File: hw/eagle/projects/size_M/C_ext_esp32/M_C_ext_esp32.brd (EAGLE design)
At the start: 19 parts, among them IC1 CP2102

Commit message: pcb M.1 -not finished
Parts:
- removed C1, C2, C4: 100n, rcl:C0603
- removed C3: 0.1F, rcl:C0603
- removed C5: 10u, rcl:C0603
- removed C6: 2u2, rcl:C0603
- removed IC1: CP2102, silabs:MLP28
- removed R1, R2: 2k2, rcl:R0603
- removed R3, R4, R5, R6: 12k, rcl:R0603
- removed T1, T2: (no value), transistor:SOT23-BEC
- removed USB: MICRO-USB, hugo:MICRO-USB
- added C.C1, C.C2, C.C4: 100n, rcl:C0603
- added C.C3: 22u, rcl:C0805
- added C.C5: 10u, rcl:C0603
- added C.C6: 2u2, rcl:C0603
- added C.R1, C.R2: 2k2, rcl:R0603
- added C.R3, C.R4, C.R5, C.R6: 12k, rcl:R0603
- added C.U1: TTGO-MICRO-32, hugo:TTGO-MICRO-32
- added C.U3: BC817DS,115, SamacSys_Parts:SOT95P275X110-6N
- added U1: CP2104-F03-GM, CP2104:QFN50P400X400X80-25N
- JP1: device pinhead2:1X02 -> pinhead2:1X04
- U$1: value TTGO-MICRO-32 -> USB-C; device hugo:TTGO-MICRO-32 -> hugo:USB-C
- moved U$1 8.85 mm to (10.5, 18.4), flipped to the bottom
- moved JP1 2.53 mm to (19.6, 10.5)
- renumbered JP2 to C.J2
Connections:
- removed net VDD: C1.1, C2.1, C3.1, IC1.6, R1.2, R2.2, R5.2, R6.1, U$1.3V3
- new net VCC: C.C1.1, C.C2.1, C.C3.1, C.R1.2, C.R2.2, C.R5.2, C.R6.1, C.U1.3V3, JP1.3, U1.6
- new net VIO: U1.5
- net GND: now also C.C1.2, C.C2.2, C.C3.2, C.C4.1, C.C5.1, C.C6.2, C.U1.GND1, C.U1.GND10, C.U1.GND11, C.U1.GND2, C.U1.GND3, C.U1.GND4, C.U1.GND5, C.U1.GND6, C.U1.GND7, C.U1.GND8, C.U1.GND9, JP1.4, U$1.A1B12, U$1.B1A12, U$1.SH1, U$1.SH2, U$1.SH3, U$1.SH4, U1.2, U1.25; no longer C1.2, C2.2, C3.2, C4.1, C5.1, C6.2, IC1.3, IC1.EXP, IC1.M, U$1.GND1, U$1.GND2, U$1.GND3, U$1.GND4, USB.GND, USB.GND1, USB.GND2, USB.GND3, USB.GND4, USB.P$1, USB.P$2
- net N$1: now also U$1.A7, U1.4; no longer IC1.5, USB.D-
- net N$10: now also C.R5.1, C.U1.IO0, C.U3.3; no longer R5.1, T2.C, U$1.IO0
- net N$11: now also C.C6.1, C.R6.2, C.U1.EN, C.U3.6; no longer C6.1, R6.2, T1.C, U$1.EN
- net N$13: now also C.U1.IO2; no longer U$1.IO2
- net N$2: now also U$1.A6, U1.3; no longer IC1.4, USB.D+
- net N$5: now also C.R4.2, C.U3.5; no longer R4.2, T1.B
- net N$7: now also C.R3.2, C.U3.2; no longer R3.2, T2.B
- net N$8: now also C.R3.1, C.U3.4, U1.19; no longer IC1.9, R3.1, T1.E
- net N$9: now also C.R4.1, C.U3.1, U1.23; no longer IC1.28, R4.1, T2.E
- net RX: now also C.U1.RXD0, U1.20; no longer IC1.25, U$1.RXD0
- net SCL: now also C.R1.1, C.U1.IO22; no longer R1.1, U$1.IO22
- net SDA: now also C.R2.1, C.U1.IO21; no longer R2.1, U$1.IO21
- net TX: now also C.U1.TXD0, U1.21; no longer IC1.26, U$1.TXD0
- net VUSB: now also C.C4.2, C.C5.2, U$1.A4B9, U$1.B4A9, U1.7, U1.8; no longer C4.2, C5.2, IC1.7, IC1.8, USB.VUSB
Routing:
- net VCC: track 0.00 -> 56.4 mm
- net VDD: track 54.9 -> 0.00 mm, vias 5 -> 0
- net N$11: track 23.4 -> 12.9 mm, vias 1 -> 2
- net N$10: track 9.96 -> 19.7 mm, vias 1 -> 2
- net GND: track 111.2 -> 119.3 mm, vias 4 -> 6
- net RX: track 13.1 -> 5.41 mm
- net N$1: track 9.82 -> 2.26 mm, vias 2 -> 0
- net VUSB: track 22.7 -> 29.8 mm, vias 2 -> 3
- net N$2: track 9.08 -> 2.25 mm
- net TX: track 12.0 -> 7.57 mm
- net N$7: track 4.91 -> 2.24 mm
- net N$9: track 13.5 -> 14.6 mm
- net N$8: track 11.2 -> 12.3 mm, vias 0 -> 2
- net N$5: track 2.51 -> 3.22 mm
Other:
- board text added: "ESP M.1"
- board text removed: "esp M.0"

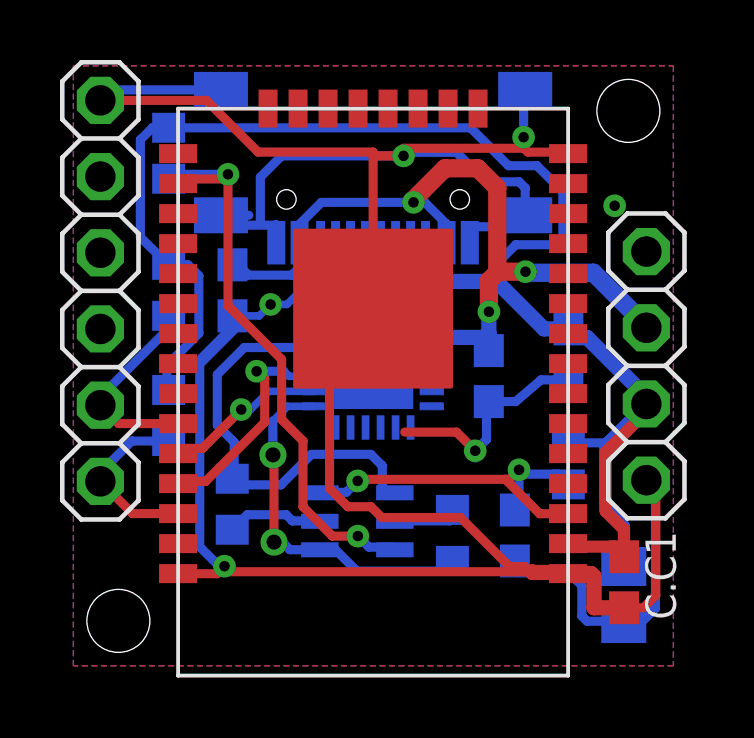
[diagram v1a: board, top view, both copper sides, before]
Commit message: updateed PCBs - adjustments based on usage of version 1
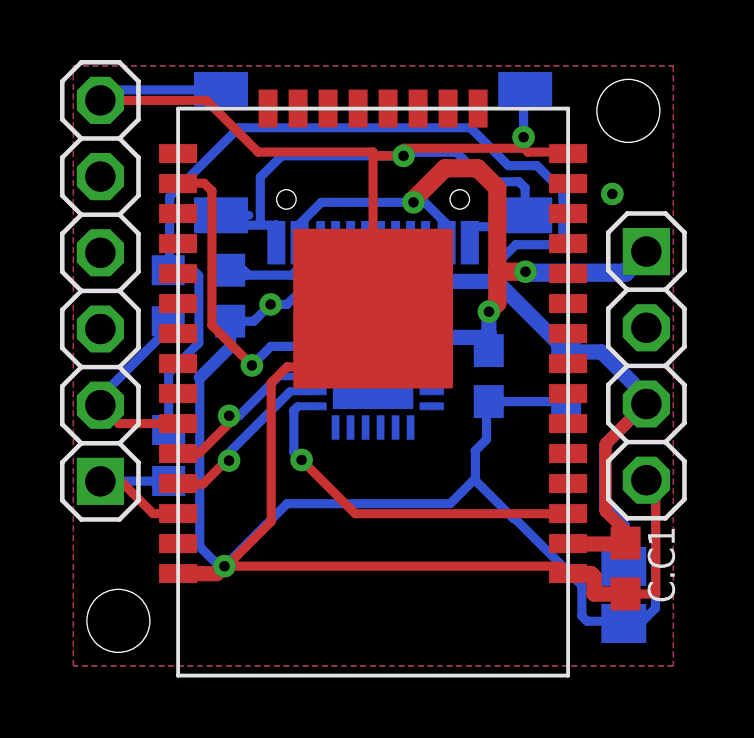
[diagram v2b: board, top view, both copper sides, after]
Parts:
- removed C.C6: 2u2, rcl:C0603
- removed C.R3, C.R4, C.R5, C.R6: 12k, rcl:R0603
- removed C.U3: BC817DS,115, SamacSys_Parts:SOT95P275X110-6N
- moved C.R1 1.33 mm to (3.68, 7.51)
- moved C.C2 0.74 mm to (16.9, 10.1)
- moved C.C1 0.46 mm to (18.9, 3.74)
- moved C.C5 0.19 mm to (5.73, 12.8)
- moved C.R2 0.18 mm to (3.66, 12.8)
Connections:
- removed net N$10: C.R5.1, C.U1.IO0, C.U3.3
- removed net N$11: C.C6.1, C.R6.2, C.U1.EN, C.U3.6
- removed net N$13: C.U1.IO2
- removed net N$5: C.R4.2, C.U3.5
- removed net N$7: C.R3.2, C.U3.2
- removed net N$8: C.R3.1, C.U3.4, U1.19
- removed net N$9: C.R4.1, C.U3.1, U1.23
- new net PROG: C.U1.IO0, U1.23
- new net RESET: C.U1.EN, U1.19
- net GND: no longer C.C6.2
- net RX: now also C.U1.TXD0; no longer C.U1.RXD0
- net TX: now also C.U1.RXD0; no longer C.U1.TXD0
- net VCC: no longer C.R5.2, C.R6.1
- net VUSB: now also JP1.1; no longer JP1.2
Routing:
- net N$10: track 19.7 -> 0.00 mm, vias 2 -> 0
- net N$9: track 14.6 -> 0.00 mm
- net N$11: track 12.9 -> 0.00 mm, vias 2 -> 0
- net N$8: track 12.3 -> 0.00 mm, vias 2 -> 0
- net RESET: track 0.00 -> 12.1 mm, vias 0 -> 1
- net GND: track 119.3 -> 130.4 mm, vias 6 -> 5
- net PROG: track 0.00 -> 9.97 mm, vias 0 -> 1
- net VCC: track 56.4 -> 53.1 mm
- net N$5: track 3.22 -> 0.00 mm
- net N$7: track 2.24 -> 0.00 mm
- net TX: track 7.57 -> 5.76 mm
- net SCL: track 6.04 -> 5.32 mm
- net RX: track 5.41 -> 5.99 mm
- net VUSB: track 29.8 -> 29.3 mm
